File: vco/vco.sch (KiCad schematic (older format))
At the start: 48 parts

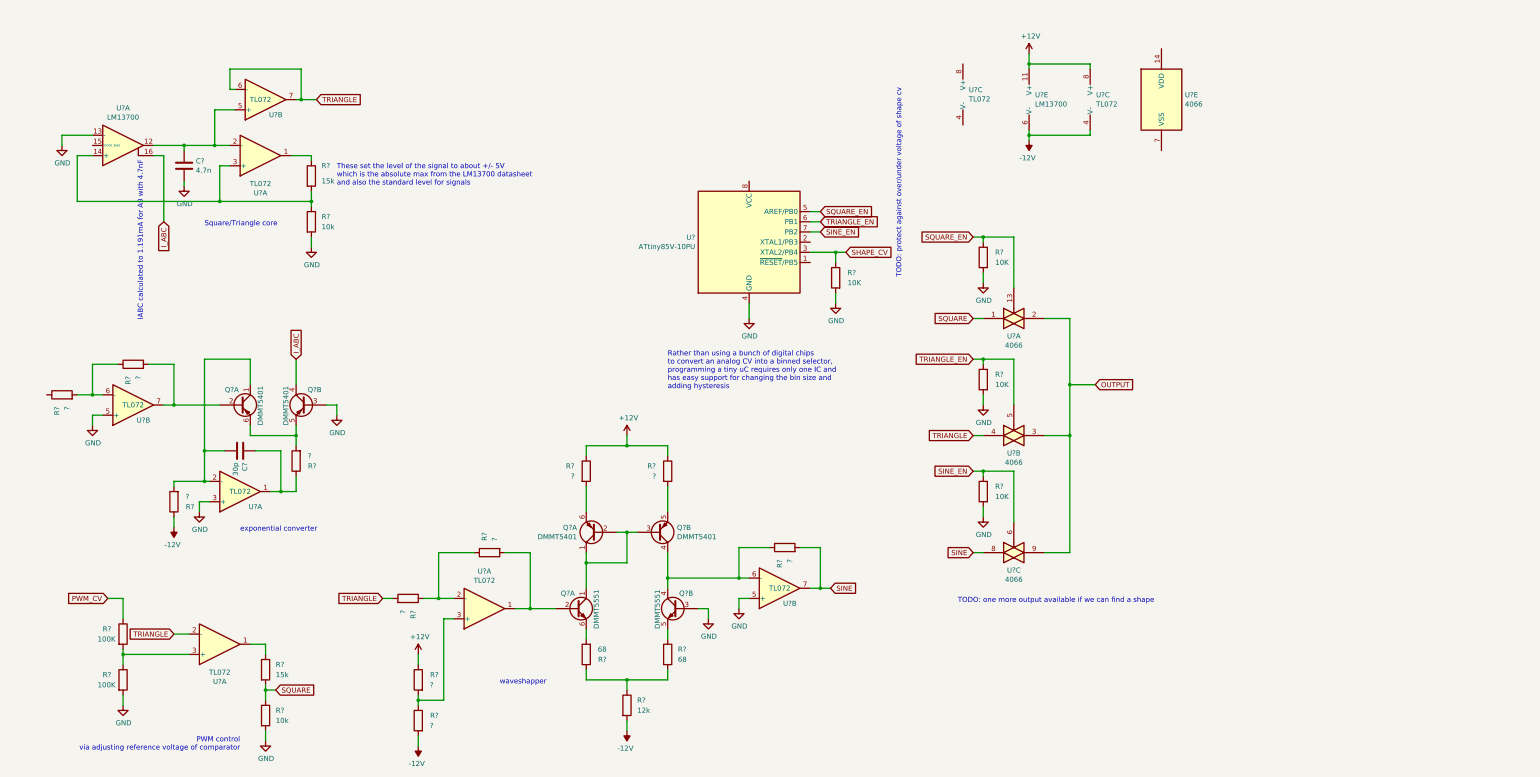
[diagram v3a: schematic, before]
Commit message: output selector CV
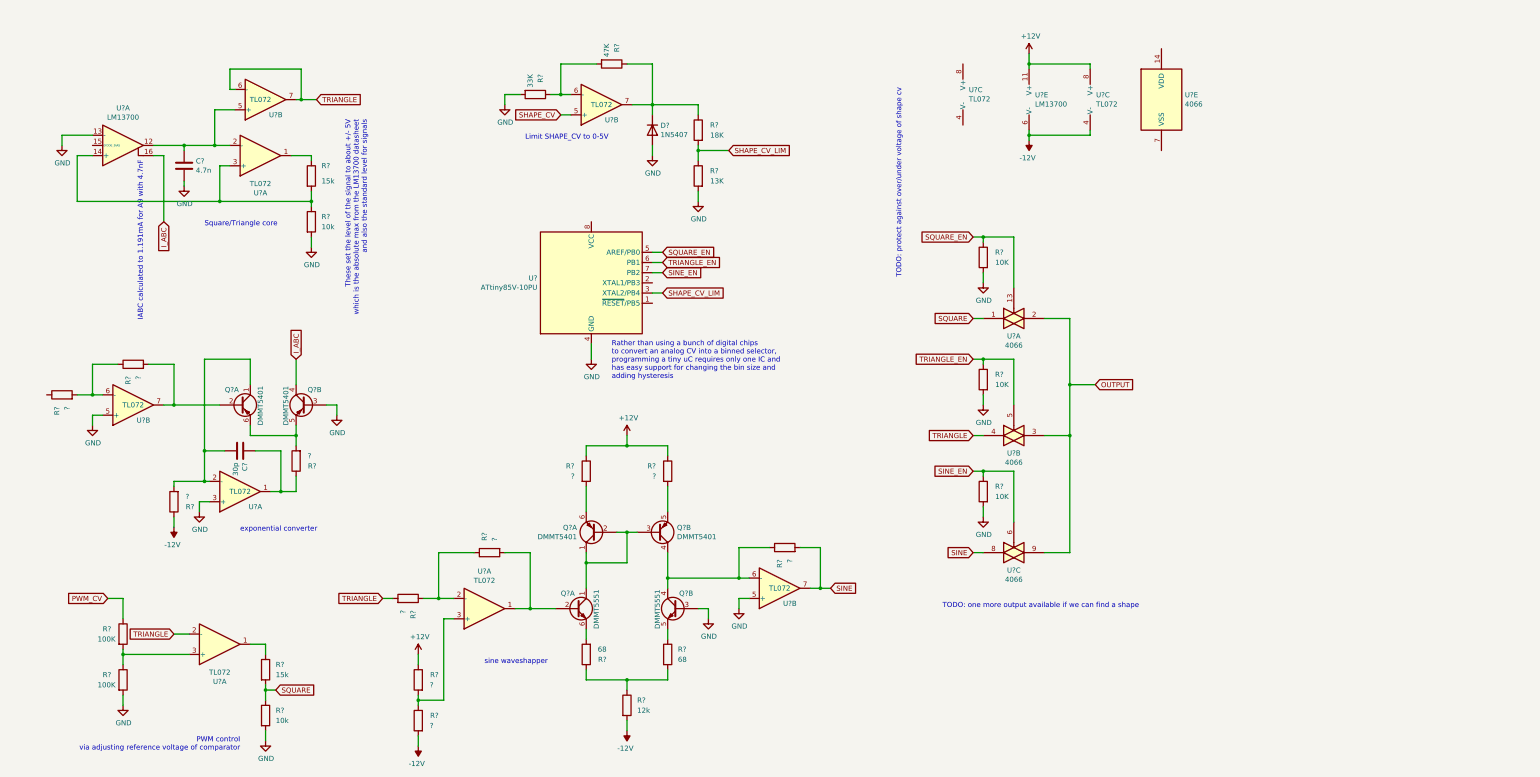
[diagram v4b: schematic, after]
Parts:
- removed R?: 10K, symbol Device:R
- added D?: 1N5407, Diode_THT:D_DO-201AD_P15.24mm_Horizontal, symbol Diode:1N5407
- added R?: 47K, symbol Device:R
- added R?: 33K, symbol Device:R
- added R?: 13K, symbol Device:R
- added R?: 18K, symbol Device:R
- added U?: TL072, symbol Amplifier_Operational:TL072
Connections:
- net GND: now also D?.2 (A), R?.2, R?.2
- net SHAPE_CV: now also U?.5 (+); no longer U?.3 (XTAL2/PB4)
- new net: R?.1, R?.2, U?.6 (-)
- new net: D?.1 (K), R?.1, R?.1, U?.7
- new net SHAPE_CV_LIM: R?.1, R?.2, U?.3 (XTAL2/PB4)
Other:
- note added: "Limit SHAPE_CV to 0-5V"
- note added: "sine waveshapper"
- note removed: "waveshapper"
- moved on the sheet: U?
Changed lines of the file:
@@
 	1    0    0    -1
 $EndComp
-Text Notes 5000 6850 0    50   ~ 0
-waveshapper
+Text Notes 4850 6650 0    50   ~ 0
+sine waveshapper
 Text GLabel 8250 5900 2    50   Input ~ 0
 SINE
@@
 	1    0    0    -1
 $EndComp
-Text Notes 3400 1950 0    50   ~ 0
+Text Notes 3700 1300 3    50   ~ 0
 These set the level of the signal to about +/- 5V\nwhich is the absolute max from the LM13700 datasheet\nand also the standard level for signals
 $Comp
@@
 L MCU_Microchip_ATtiny:ATtiny85V-10PU U?
 U 1 1 5F04221D
-P 7450 2500
-F 0 "U?" H 6920 2546 50  0000 R CNN
-F 1 "ATtiny85V-10PU" H 6920 2455 50  0000 R CNN
-F 2 "Package_DIP:DIP-8_W7.62mm" H 7450 2500 50  0001 C CIN
-F 3 "http://ww1.microchip.com/downloads/en/DeviceDoc/atmel-2586-avr-8-bit-microcontroller-attiny25-attiny45-attiny85_datasheet.pdf" H 7450 2500 50  0001 C CNN
-	1    7450 2500
+P 5900 2900
+F 0 "U?" H 5370 2946 50  0000 R CNN
+F 1 "ATtiny85V-10PU" H 5370 2855 50  0000 R CNN
+F 2 "Package_DIP:DIP-8_W7.62mm" H 5900 2900 50  0001 C CIN
+F 3 "http://ww1.microchip.com/downloads/en/DeviceDoc/atmel-2586-avr-8-bit-microcontroller-attiny25-attiny45-attiny85_datasheet.pdf" H 5900 2900 50  0001 C CNN
+	1    5900 2900
 	1    0    0    -1
 $EndComp
@@
 L power:GND #PWR?
 U 1 1 5F1156A6
-P 7450 3250
-F 0 "#PWR?" H 7450 3000 50  0001 C CNN
-F 1 "GND" H 7455 3077 50  0000 C CNN
-F 2 "" H 7450 3250 50  0001 C CNN
-F 3 "" H 7450 3250 50  0001 C CNN
-	1    7450 3250
-	1    0    0    -1
-$EndComp
-Wire Wire Line
-	7450 3100 7450 3250
-Text GLabel 8150 2200 2    50   Input ~ 0
+P 5900 3650
+F 0 "#PWR?" H 5900 3400 50  0001 C CNN
+F 1 "GND" H 5905 3477 50  0000 C CNN
+F 2 "" H 5900 3650 50  0001 C CNN
+F 3 "" H 5900 3650 50  0001 C CNN
+	1    5900 3650
+	1    0    0    -1
+$EndComp
+Wire Wire Line
+	5900 3500 5900 3650
+Text GLabel 6600 2600 2    50   Input ~ 0
 SQUARE_EN
-Text GLabel 8150 2300 2    50   Input ~ 0
+Text GLabel 6600 2700 2    50   Input ~ 0
 TRIANGLE_EN
-Text GLabel 8150 2400 2    50   Input ~ 0
+Text GLabel 6600 2800 2    50   Input ~ 0
 SINE_EN
-Text GLabel 8400 2600 2    50   Input ~ 0
+Text GLabel 5600 1250 0    50   Input ~ 0
 SHAPE_CV
-$Comp
-L Device:R R?
-U 1 1 5F11D91C
-P 8300 2850
-F 0 "R?" H 8100 2900 50  0000 L CNN
-F 1 "10K" H 8050 2800 50  0000 L CNN
-F 2 "" V 8230 2850 50  0001 C CNN
-F 3 "~" H 8300 2850 50  0001 C CNN
-	1    8300 2850
-	-1   0    0    -1
-$EndComp
-$Comp
-L power:GND #PWR?
-U 1 1 5F11EAE5
-P 8300 3100
-F 0 "#PWR?" H 8300 2850 50  0001 C CNN
-F 1 "GND" H 8305 2927 50  0000 C CNN
-F 2 "" H 8300 3100 50  0001 C CNN
-F 3 "" H 8300 3100 50  0001 C CNN
-	1    8300 3100
-	1    0    0    -1
-$EndComp
-Wire Wire Line
-	8300 3100 8300 3000
-Wire Wire Line
-	8300 2700 8300 2600
-Wire Wire Line
-	8300 2600 8400 2600
-Wire Wire Line
-	8300 2600 8050 2600
-Connection ~ 8300 2600
-Wire Wire Line
-	8150 2400 8050 2400
-Wire Wire Line
-	8150 2300 8050 2300
-Wire Wire Line
-	8050 2200 8150 2200
-Text Notes 6650 3950 0    50   ~ 0
+Wire Wire Line
+	6600 2800 6500 2800
+Wire Wire Line
+	6600 2700 6500 2700
+Wire Wire Line
+	6500 2600 6600 2600
+Text Notes 6100 3850 0    50   ~ 0
 Rather than using a bunch of digital chips\nto convert an analog CV into a binned selector,\nprogramming a tiny uC requires only one IC and\nhas easy support for changing the bin size and\nadding hysteresis
 $Comp
@@
 Text Notes 2450 7500 2    50   ~ 0
 PWM control\nvia adjusting reference voltage of comparator
-Text Notes 9500 6050 0    50   ~ 0
+Text Notes 9350 6100 0    50   ~ 0
 TODO: one more output available if we can find a shape
 Text Notes 8950 2850 1    50   ~ 0
 TODO: protect against over/under voltage of shape cv
+$Comp
+L Amplifier_Operational:TL072 U?
+U 2 1 5F1C6C70
+P 6000 1150
+F 0 "U?" H 6100 1300 50  0000 C CNN
+F 1 "TL072" H 6000 1150 50  0000 C CNN
+F 2 "" H 6000 1150 50  0001 C CNN
+F 3 "http://www.ti.com/lit/ds/symlink/tl071.pdf" H 6000 1150 50  0001 C CNN
+	2    6000 1150
+	1    0    0    1
+$EndComp
+$Comp
+L power:GND #PWR?
+U 1 1 5F1CFF2C
+P 5050 1150
+F 0 "#PWR?" H 5050 900 50  0001 C CNN
+F 1 "GND" H 5055 977 50  0000 C CNN
+F 2 "" H 5050 1150 50  0001 C CNN
+F 3 "" H 5050 1150 50  0001 C CNN
+	1    5050 1150
+	1    0    0    -1
+$EndComp
+$Comp
+L power:GND #PWR?
+U 1 1 5F1D03C7
+P 6950 2100
+F 0 "#PWR?" H 6950 1850 50  0001 C CNN
+F 1 "GND" H 6955 1927 50  0000 C CNN
+F 2 "" H 6950 2100 50  0001 C CNN
+F 3 "" H 6950 2100 50  0001 C CNN
+	1    6950 2100
+	1    0    0    -1
+$EndComp
+$Comp
+L Device:R R?
+U 1 1 5F1D08FB
+P 6950 1850
+F 0 "R?" H 6750 1900 50  0000 L CNN
+F 1 "13K" H 6700 1800 50  0000 L CNN
+F 2 "" V 6880 1850 50  0001 C CNN
+F 3 "~" H 6950 1850 50  0001 C CNN
+	1    6950 1850
+	-1   0    0    -1
+$EndComp
+$Comp
+L Device:R R?
+U 1 1 5F1D0EBF
+P 6950 1400
+F 0 "R?" H 6750 1450 50  0000 L CNN
+F 1 "18K" H 6700 1350 50  0000 L CNN
+F 2 "" V 6880 1400 50  0001 C CNN
+F 3 "~" H 6950 1400 50  0001 C CNN
+	1    6950 1400
+	-1   0    0    -1
+$EndComp
+Wire Wire Line
+	5050 1150 5050 1050
+Wire Wire Line
+	5050 1050 5200 1050
+Wire Wire Line
+	5500 1050 5600 1050
+Wire Wire Line
+	5600 1050 5600 750
+Wire Wire Line
+	5600 750  5950 750
+Connection ~ 5600 1050
+Wire Wire Line
+	5600 1050 5700 1050
+Wire Wire Line
+	5600 1250 5700 1250
+Wire Wire Line
+	6950 2100 6950 2000
+Wire Wire Line
+	6950 1700 6950 1600
+Wire Wire Line
+	6500 1150 6300 1150
+Wire Wire Line
+	6250 750  6500 750
+Wire Wire Line
+	6500 750  6500 1150
+$Comp
+L Diode:1N5407 D?
+U 1 1 5F22202A
+P 6500 1400
+F 0 "D?" V 6454 1479 50  0000 L CNN
+F 1 "1N5407" V 6545 1479 50  0000 L CNN
+F 2 "Diode_THT:D_DO-201AD_P15.24mm_Horizontal" H 6500 1225 50  0001 C CNN
+F 3 "http://www.vishay.com/docs/88516/1n5400.pdf" H 6500 1400 50  0001 C CNN
+	1    6500 1400
+	0    1    1    0
+$EndComp
+$Comp
+L power:GND #PWR?
+U 1 1 5F22CC2B
+P 6500 1650
+F 0 "#PWR?" H 6500 1400 50  0001 C CNN
+F 1 "GND" H 6505 1477 50  0000 C CNN
+F 2 "" H 6500 1650 50  0001 C CNN
+F 3 "" H 6500 1650 50  0001 C CNN
+	1    6500 1650
+	1    0    0    -1
+$EndComp
+Wire Wire Line
+	6500 1650 6500 1550
+$Comp
+L Device:R R?
+U 1 1 5F1CEAF3
+P 6100 750
+F 0 "R?" H 5900 800 50  0000 L CNN
+F 1 "47K" H 5900 700 50  0000 L CNN
+F 2 "" V 6030 750 50  0001 C CNN
+F 3 "~" H 6100 750 50  0001 C CNN
+	1    6100 750
+	0    1    1    0
+$EndComp
+$Comp
+L Device:R R?
+U 1 1 5F1CF634
+P 5350 1050
+F 0 "R?" H 5150 1100 50  0000 L CNN
+F 1 "33K" H 5150 1000 50  0000 L CNN
+F 2 "" V 5280 1050 50  0001 C CNN
+F 3 "~" H 5350 1050 50  0001 C CNN
+	1    5350 1050
+	0    1    1    0
+$EndComp
+Text GLabel 7250 1600 2    50   Input ~ 0
+SHAPE_CV_LIM
+Text GLabel 6600 3000 2    50   Input ~ 0
+SHAPE_CV_LIM
+Wire Wire Line
+	6600 3000 6500 3000
+Text Notes 5250 1500 0    50   ~ 0
+Limit SHAPE_CV to 0-5V
+Wire Wire Line
+	6500 1250 6500 1150
+Connection ~ 6500 1150
+Wire Wire Line
+	6950 1250 6950 1150
+Wire Wire Line
+	6950 1150 6500 1150
+Wire Wire Line
+	7250 1600 6950 1600
+Connection ~ 6950 1600
+Wire Wire Line
+	6950 1600 6950 1550
 $EndSCHEMATC

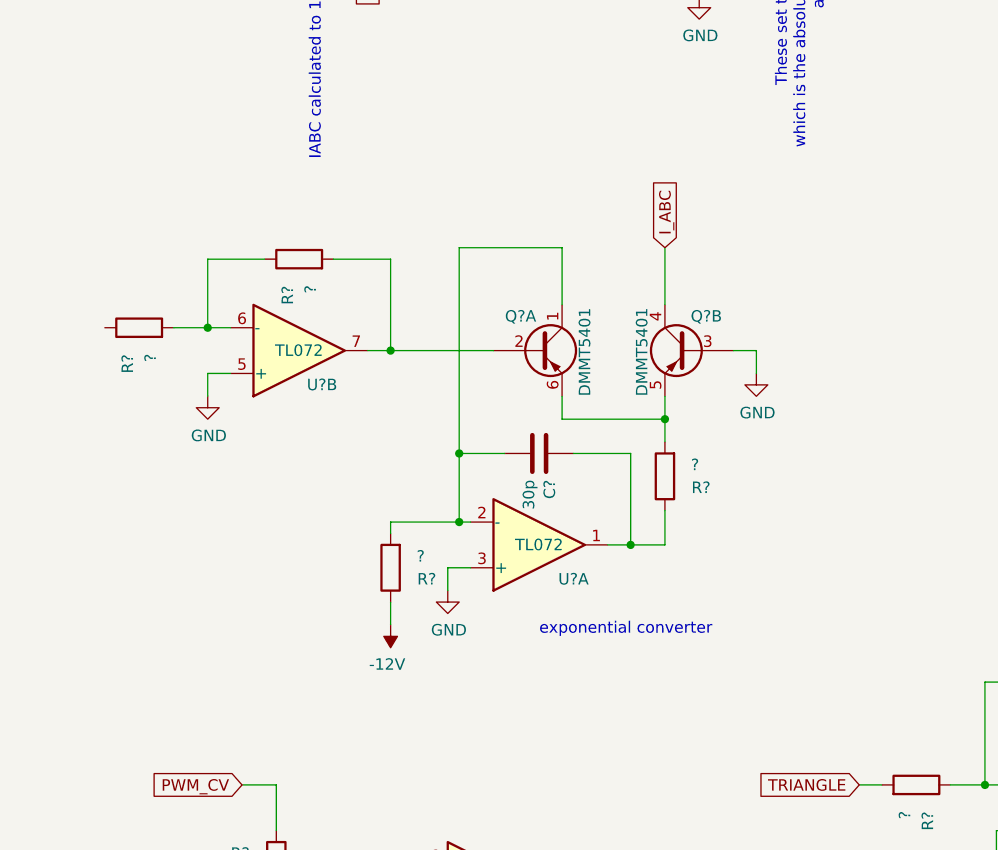
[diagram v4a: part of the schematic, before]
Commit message: updated vco calculations
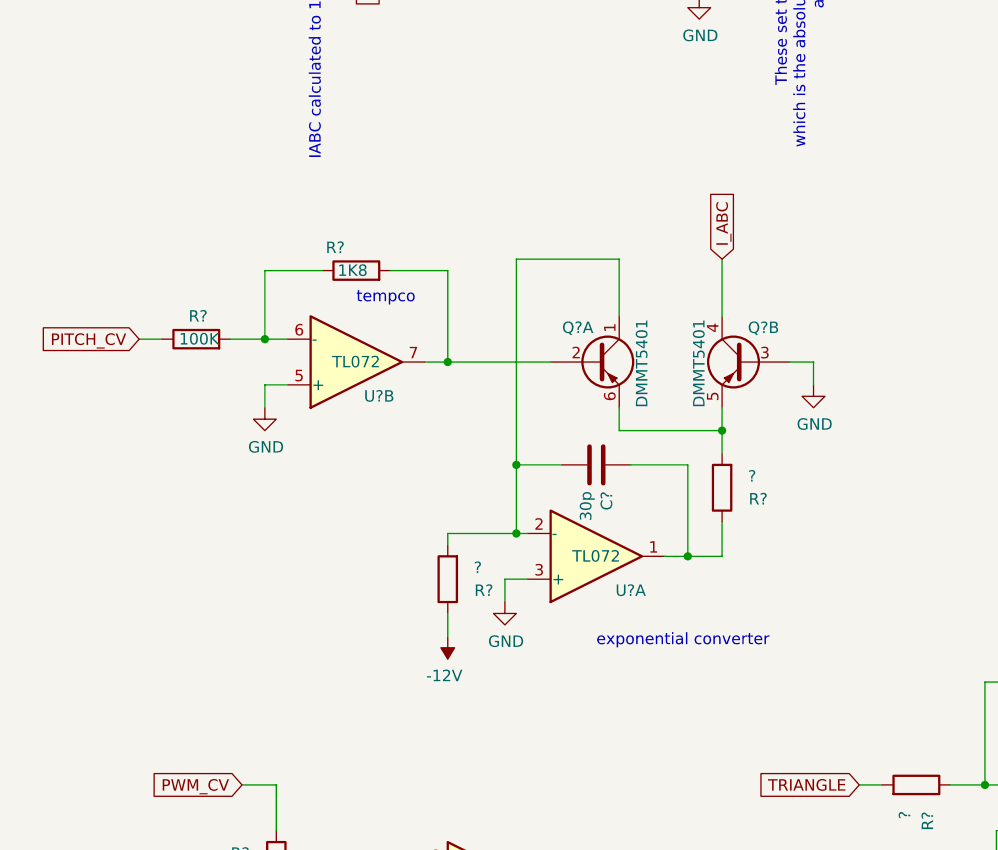
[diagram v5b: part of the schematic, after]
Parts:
- R?: value ? -> 1K8
- R?: value ? -> 100K
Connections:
- net PITCH_CV: now reaches R?.1
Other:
- note added: "tempco"
- moved on the sheet: C?, Q?A, Q?B, R?, U?A, U?B

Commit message: experimenting with error
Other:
- note added: "These set the level of the signal to about +/- 5V\nwhich is the absolute max from the LM13700 datasheet\nand also the standard level for signals\n\nTODO: unbalanced voltage outputs causes error in the frequency.\nNeed to find a way to compensate for this"
- note removed: "These set the level of the signal to about +/- 5V\nwhich is the absolute max from the LM13700 datasheet\nand also the standard level for signals"
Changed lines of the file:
@@
 	1    0    0    -1
 $EndComp
-Text Notes 3700 1300 3    50   ~ 0
-These set the level of the signal to about +/- 5V\nwhich is the absolute max from the LM13700 datasheet\nand also the standard level for signals
+Text Notes 3850 1300 3    50   ~ 0
+These set the level of the signal to about +/- 5V\nwhich is the absolute max from the LM13700 datasheet\nand also the standard level for signals\n\nTODO: unbalanced voltage outputs causes error in the frequency.\nNeed to find a way to compensate for this
 $Comp
 L power:GND #PWR?
